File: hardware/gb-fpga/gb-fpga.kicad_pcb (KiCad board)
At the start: 4 copper layers, 80.1 x 78.6 mm, 20 parts, among them J1 USB_C_Receptacle_USB2.0, J2 Cartridge-32pin, U1 xc7s25ftgb196, U2 MX25R3235FZBxx1, U3 FT2232HQ

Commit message: Add USB connections
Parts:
- added R10: 10k, Resistor_SMD:R_0603_1608Metric, F.Cu at (11.0, -48.4)
- added R11: 10k, Resistor_SMD:R_0603_1608Metric, F.Cu at (11.0, -45.9)
- added R12: 10k, Resistor_SMD:R_0603_1608Metric, F.Cu at (15.0, -48.4)
- added R13: 10k, Resistor_SMD:R_0603_1608Metric, F.Cu at (11.0, -43.3)
- added R14: 12k, Resistor_SMD:R_0603_1608Metric, F.Cu at (15.0, -45.9)
- added R15: 1k, Resistor_SMD:R_0603_1608Metric, F.Cu at (19.0, -48.4)
- added R16: 4.7k, Resistor_SMD:R_0603_1608Metric, F.Cu at (15.0, -43.3)
- added R17: 4.7k, Resistor_SMD:R_0603_1608Metric, F.Cu at (19.0, -45.9)
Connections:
- J1 pad A1: Net-(J1-PadA1) -> GND
- J1 pad A12: Net-(J1-PadA1) -> GND
- J1 pad B1: Net-(J1-PadA1) -> GND
- J1 pad B12: Net-(J1-PadA1) -> GND
- J1 pad B6: Net-(J1-PadB6) -> Net-(J1-PadA6)
- J1 pad B7: Net-(J1-PadB7) -> Net-(J1-PadA7)
- J1 pad S1: Net-(J1-PadS1) -> GND
- U1 pad A12: (no net) -> Net-(U1-PadA12)
- U1 pad A13: (no net) -> Net-(U1-PadA13)
- U1 pad A2: (no net) -> Net-(U1-PadA2)
- U1 pad A3: (no net) -> Net-(U1-PadA3)
- U1 pad A4: (no net) -> Net-(U1-PadA4)
- U1 pad A5: (no net) -> Net-(U1-PadA5)
- U1 pad A7: Net-(U1-PadA7) -> TCK
- U1 pad B1: (no net) -> Net-(U1-PadB1)
- U1 pad B13: (no net) -> Net-(U1-PadB13)
- U1 pad B14: (no net) -> Net-(U1-PadB14)
- U1 pad B2: (no net) -> Net-(U1-PadB2)
- U1 pad B3: (no net) -> Net-(U1-PadB3)
- U1 pad B5: (no net) -> Net-(U1-PadB5)
- U1 pad B6: (no net) -> Net-(U1-PadB6)
- U1 pad C1: (no net) -> Net-(U1-PadC1)
- U1 pad C12: (no net) -> Net-(U1-PadC12)
- U1 pad C14: (no net) -> Net-(U1-PadC14)
- U1 pad C3: (no net) -> Net-(U1-PadC3)
- U1 pad C4: (no net) -> Net-(U1-PadC4)
- U1 pad C5: (no net) -> Net-(U1-PadC5)
- U1 pad D1: (no net) -> Net-(U1-PadD1)
- U1 pad D12: (no net) -> Net-(U1-PadD12)
- U1 pad D13: (no net) -> Net-(U1-PadD13)
- U1 pad D14: (no net) -> Net-(U1-PadD14)
- U1 pad D2: (no net) -> Net-(U1-PadD2)
- U1 pad D3: (no net) -> Net-(U1-PadD3)
- U1 pad D4: (no net) -> Net-(U1-PadD4)
- U1 pad E11: (no net) -> Net-(U1-PadE11)
- U1 pad E12: (no net) -> Net-(U1-PadE12)
- U1 pad E13: (no net) -> Net-(U1-PadE13)
- U1 pad E2: (no net) -> Net-(U1-PadE2)
- U1 pad E4: (no net) -> Net-(U1-PadE4)
- U1 pad F1: (no net) -> RX
- U1 pad F11: (no net) -> Net-(U1-PadF11)
- U1 pad F12: (no net) -> Net-(U1-PadF12)
- U1 pad F13: (no net) -> Net-(U1-PadF13)
- U1 pad F14: (no net) -> Net-(U1-PadF14)
- U1 pad F2: (no net) -> Net-(U1-PadF2)
- U1 pad F3: (no net) -> Net-(U1-PadF3)
- U1 pad F4: (no net) -> Net-(U1-PadF4)
- U1 pad G1: (no net) -> TX
- U1 pad G11: (no net) -> Net-(U1-PadG11)
- U1 pad G14: (no net) -> Net-(U1-PadG14)
- U1 pad G4: (no net) -> Net-(U1-PadG4)
- U1 pad H1: (no net) -> Net-(U1-PadH1)
- U1 pad H11: (no net) -> Net-(U1-PadH11)
- U1 pad H12: (no net) -> Net-(U1-PadH12)
- U1 pad H13: (no net) -> Net-(U1-PadH13)
- U1 pad H14: (no net) -> Net-(U1-PadH14)
- U1 pad H2: (no net) -> Net-(U1-PadH2)
- U1 pad H3: (no net) -> Net-(U1-PadH3)
- U1 pad H4: (no net) -> Net-(U1-PadH4)
- U1 pad J1: (no net) -> Net-(U1-PadJ1)
- U1 pad J11: (no net) -> Net-(U1-PadJ11)
- U1 pad J12: (no net) -> Net-(U1-PadJ12)
- U1 pad J13: (no net) -> Net-(U1-PadJ13)
- U1 pad J14: (no net) -> Net-(U1-PadJ14)
- U1 pad J2: (no net) -> Net-(U1-PadJ2)
- U1 pad J3: (no net) -> Net-(U1-PadJ3)
- U1 pad J4: (no net) -> Net-(U1-PadJ4)
- U1 pad K11: (no net) -> Net-(U1-PadK11)
- U1 pad K12: (no net) -> Net-(U1-PadK12)
- U1 pad K3: (no net) -> Net-(U1-PadK3)
- U1 pad K4: (no net) -> Net-(U1-PadK4)
- U1 pad L1: (no net) -> Net-(U1-PadL1)
- U1 pad L12: (no net) -> Net-(U1-PadL12)
- U1 pad L13: (no net) -> Net-(U1-PadL13)
- U1 pad L14: (no net) -> Net-(U1-PadL14)
- U1 pad L2: (no net) -> Net-(U1-PadL2)
- U1 pad L3: (no net) -> Net-(U1-PadL3)
- U1 pad L5: (no net) -> Net-(U1-PadL5)
- U1 pad M1: (no net) -> Net-(U1-PadM1)
- U1 pad M10: (no net) -> Net-(U1-PadM10)
- U1 pad M11: (no net) -> Net-(U1-PadM11)
- U1 pad M12: (no net) -> Net-(U1-PadM12)
- U1 pad M13: (no net) -> Net-(U1-PadM13)
- U1 pad M14: (no net) -> Net-(U1-PadM14)
- U1 pad M2: (no net) -> Net-(U1-PadM2)
- U1 pad M3: (no net) -> Net-(U1-PadM3)
- U1 pad M4: (no net) -> Net-(U1-PadM4)
- U1 pad M5: (no net) -> Net-(U1-PadM5)
- U1 pad M6: Net-(U1-PadM6) -> TMS
- U1 pad N1: (no net) -> Net-(U1-PadN1)
- U1 pad N10: (no net) -> Net-(U1-PadN10)
- U1 pad N11: (no net) -> Net-(U1-PadN11)
- U1 pad N14: (no net) -> Net-(U1-PadN14)
- U1 pad N4: (no net) -> Net-(U1-PadN4)
- U1 pad P10: (no net) -> Net-(U1-PadP10)
- U1 pad P11: (no net) -> Net-(U1-PadP11)
- U1 pad P12: (no net) -> Net-(U1-PadP12)
- U1 pad P13: (no net) -> Net-(U1-PadP13)
- U1 pad P2: (no net) -> Net-(U1-PadP2)
- U1 pad P3: (no net) -> Net-(U1-PadP3)
- U1 pad P4: (no net) -> Net-(U1-PadP4)
- U1 pad P5: (no net) -> Net-(U1-PadP5)
- U1 pad P6: Net-(U1-PadP6) -> TDO
- U1 pad P7: Net-(U1-PadP7) -> TDI
- U3 pad 10: Net-(U3-Pad10) -> GND
- U3 pad 13: Net-(U3-Pad13) -> GND
- U3 pad 16: Net-(U3-Pad16) -> TCK
- U3 pad 17: Net-(U3-Pad17) -> TDI
- U3 pad 18: Net-(U3-Pad18) -> TDO
- U3 pad 19: Net-(U3-Pad19) -> TMS
- U3 pad 38: Net-(U3-Pad38) -> TX
- U3 pad 39: Net-(U3-Pad39) -> RX
- U3 pad 7: Net-(U3-Pad7) -> Net-(J1-PadA7)
- U3 pad 8: Net-(U3-Pad8) -> Net-(J1-PadA6)

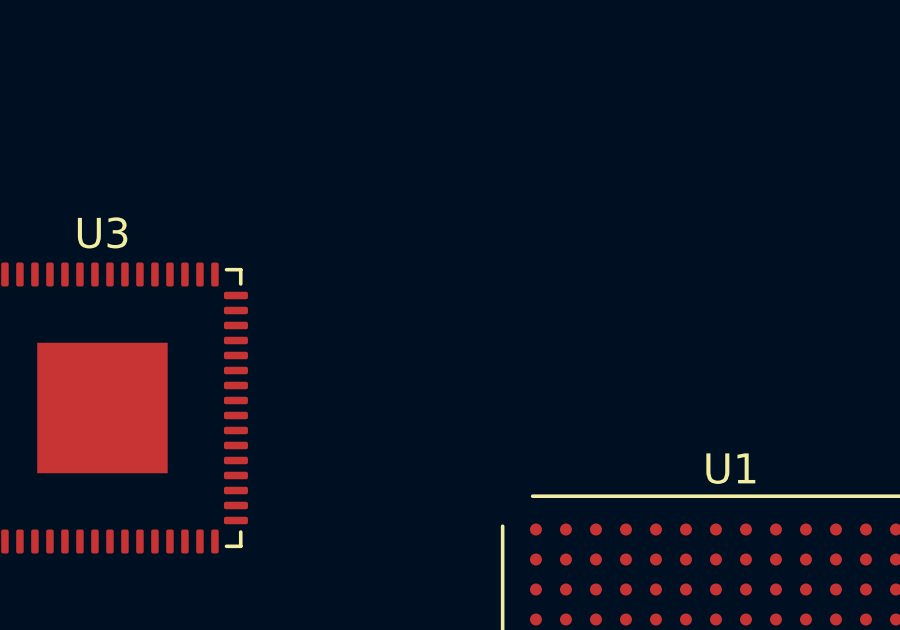
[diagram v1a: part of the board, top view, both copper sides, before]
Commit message: Add oscillator
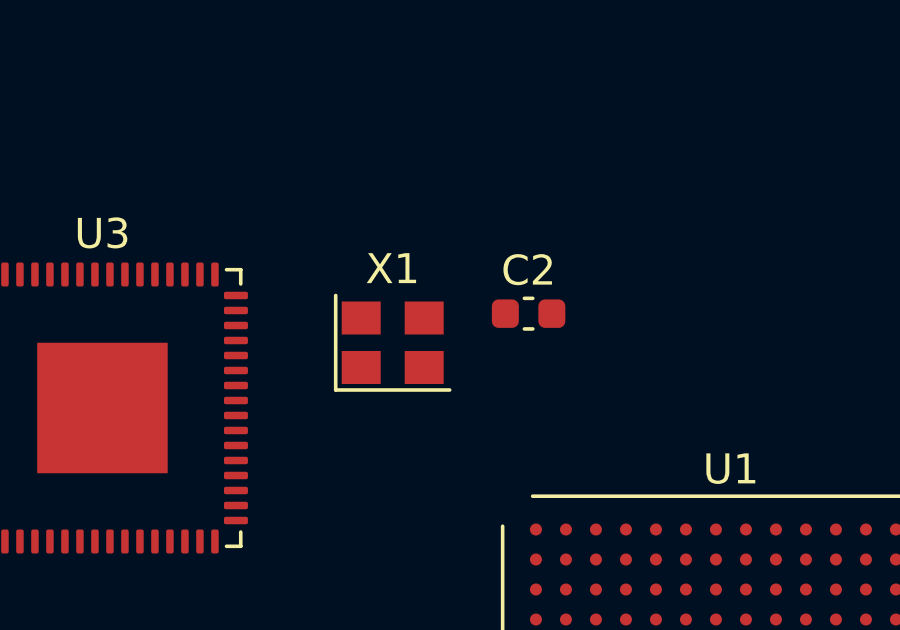
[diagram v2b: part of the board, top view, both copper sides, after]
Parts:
- added C2: 10nF, Capacitor_SMD:C_0603_1608Metric, F.Cu at (33.1, -61.1)
- added X1: SG-8002JA, Oscillator:Oscillator_SMD_Abracon_ASE-4Pin_3.2x2.5mm, F.Cu at (28.6, -60.1)
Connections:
- U1 pad H3: Net-(U1-PadH3) -> 12MHZ
- U3 pad 2: Net-(U3-Pad2) -> 12MHZ

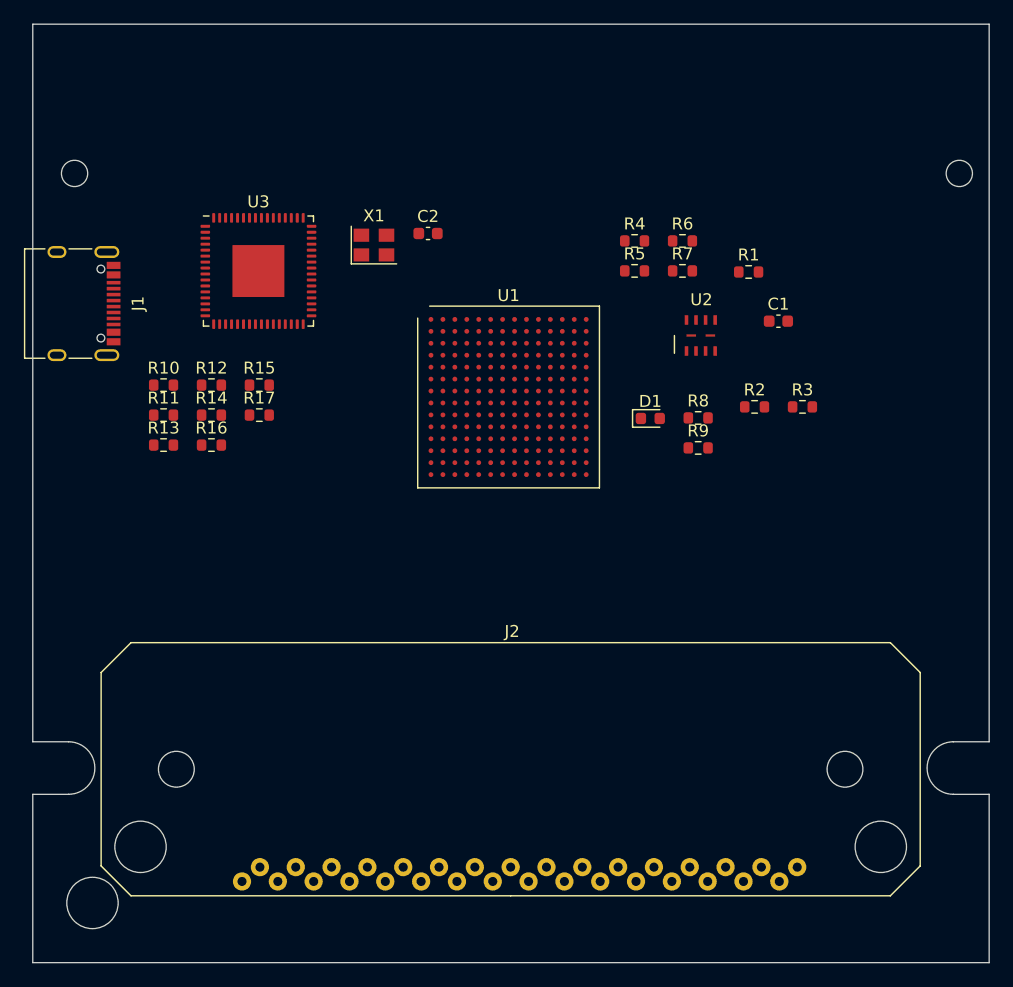
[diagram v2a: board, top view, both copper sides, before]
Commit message: Add LTC3555
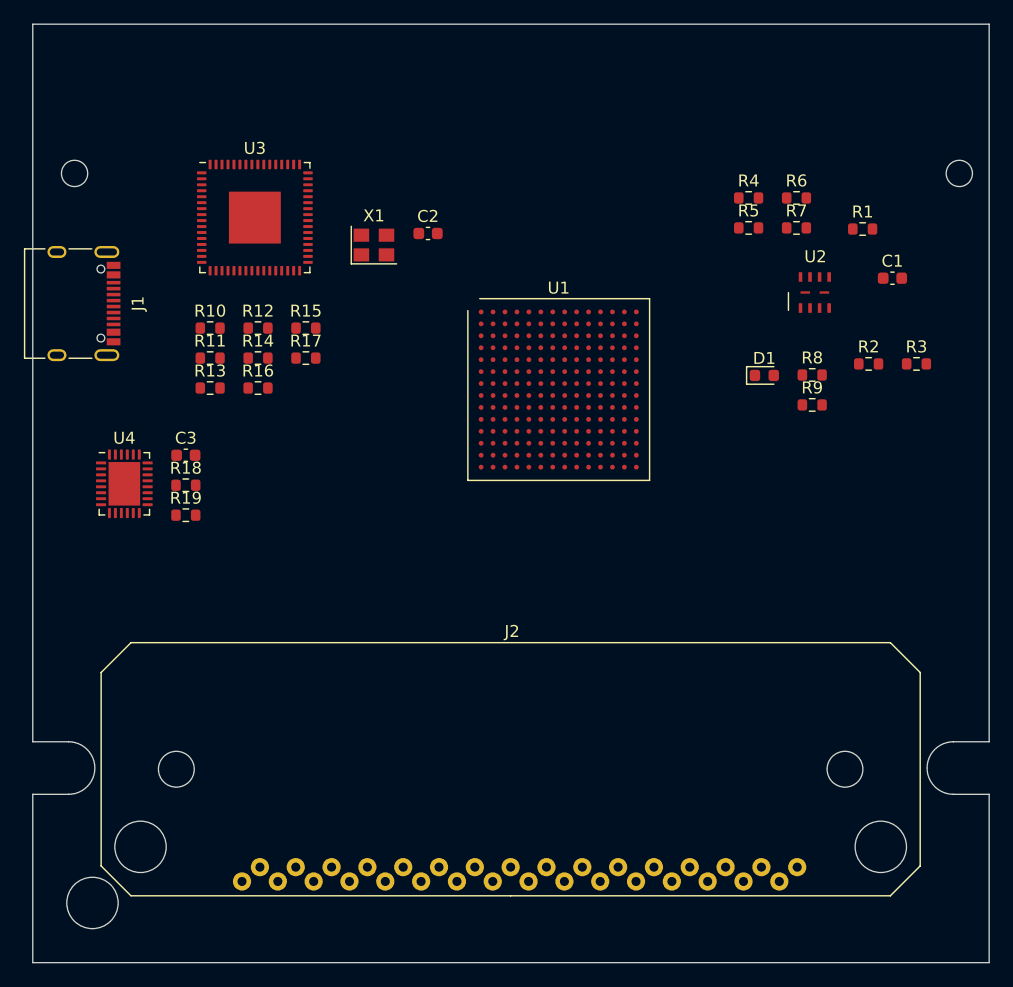
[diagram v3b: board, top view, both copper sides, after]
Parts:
- added C3: 470nF, Capacitor_SMD:C_0603_1608Metric, F.Cu at (12.8, -42.5)
- added R18: 3k, Resistor_SMD:R_0603_1608Metric, F.Cu at (12.8, -40.0)
- added R19: 2k, Resistor_SMD:R_0603_1608Metric, F.Cu at (12.8, -37.5)
- added U4: LTC3555, Package_DFN_QFN:QFN-28-1EP_4x5mm_P0.5mm_EP2.65x3.65mm, F.Cu at (7.67, -40.1)
- moved R4 10.2 mm to (60.0, -64.0)
- moved R5 10.2 mm to (60.0, -61.5)
- moved R6 10.2 mm to (64.0, -64.0)
- moved R7 10.2 mm to (64.0, -61.5)
- moved C1 10.2 mm to (72.0, -57.3)
- moved D1 10.2 mm to (61.3, -49.2)
- moved R3 10.2 mm to (74.0, -50.1)
- moved R8 10.2 mm to (65.3, -49.2)
- moved R9 10.2 mm to (65.3, -46.7)
- moved U2 10.2 mm to (65.5, -56.1)
- moved R1 10.2 mm to (69.5, -61.4)
- moved R2 10.2 mm to (70.0, -50.1)
- moved R13 6.17 mm to (14.9, -48.1)
- moved R16 6.17 mm to (18.9, -48.1)
- moved R15 6.17 mm to (22.9, -53.1)
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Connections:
- net Net-(J1-PadA4) renamed USB_5V
- net Net-(J2-Pad1) renamed +5V
- net Net-(J2-Pad10) renamed GB_A4
- net Net-(J2-Pad11) renamed GB_A5
- net Net-(J2-Pad12) renamed GB_A6
- net Net-(J2-Pad13) renamed GB_A7
- net Net-(J2-Pad14) renamed GB_A8
- net Net-(J2-Pad15) renamed GB_A9
- net Net-(J2-Pad16) renamed GB_A10
- net Net-(J2-Pad17) renamed GB_A11
- net Net-(J2-Pad18) renamed GB_A12
- net Net-(J2-Pad19) renamed GB_A13
- net Net-(J2-Pad20) renamed GB_A14
- net Net-(J2-Pad21) renamed GB_CS
- net Net-(J2-Pad22) renamed GB_D0
- net Net-(J2-Pad23) renamed GB_D1
- net Net-(J2-Pad24) renamed GB_D2
- net Net-(J2-Pad25) renamed GB_D3
- net Net-(J2-Pad26) renamed GB_D4
- net Net-(J2-Pad27) renamed GB_D5
- net Net-(J2-Pad28) renamed GB_D6
- net Net-(J2-Pad29) renamed GB_D7
- net Net-(J2-Pad3) renamed GB_RST
- net Net-(J2-Pad30) renamed GB_RD
- net Net-(J2-Pad4) renamed GB_WR
- net Net-(J2-Pad6) renamed GB_A0
- net Net-(J2-Pad7) renamed GB_A1
- net Net-(J2-Pad8) renamed GB_A2
- net Net-(J2-Pad9) renamed GB_A3

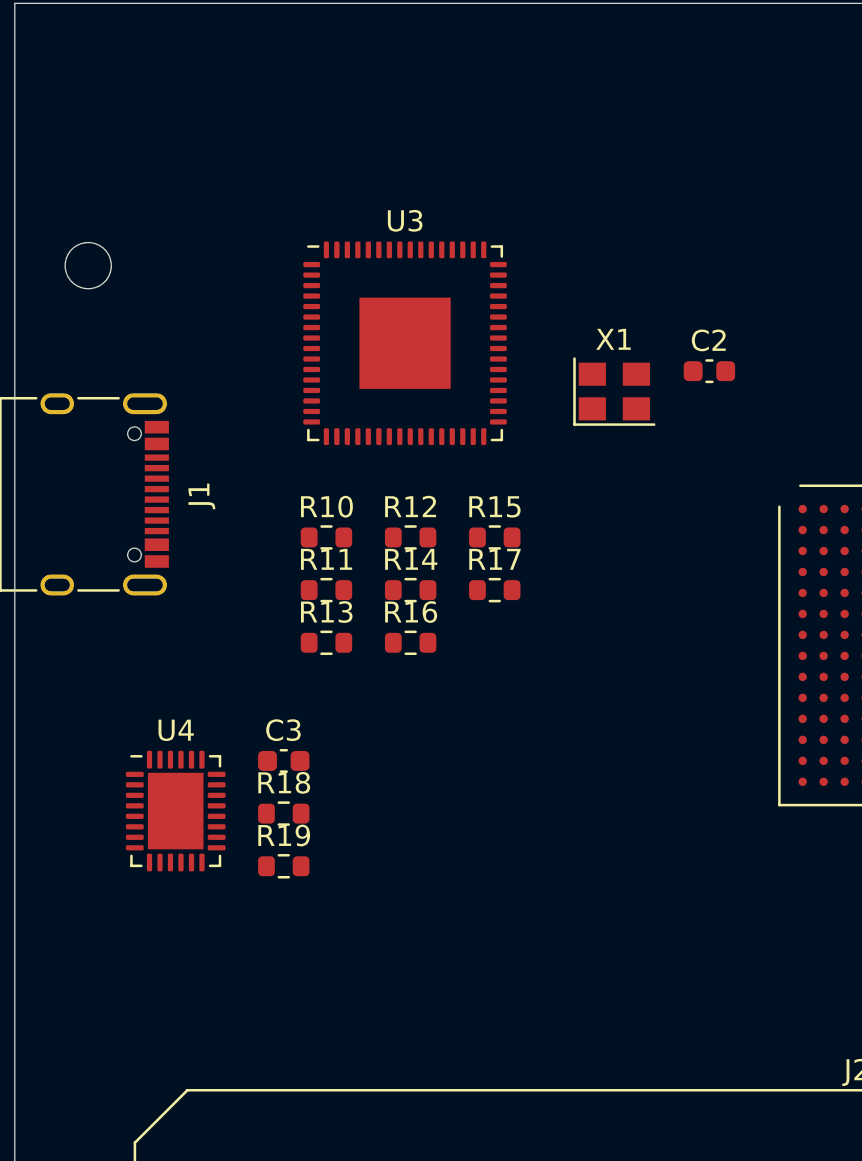
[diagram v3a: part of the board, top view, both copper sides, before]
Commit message: Add step-down conversion
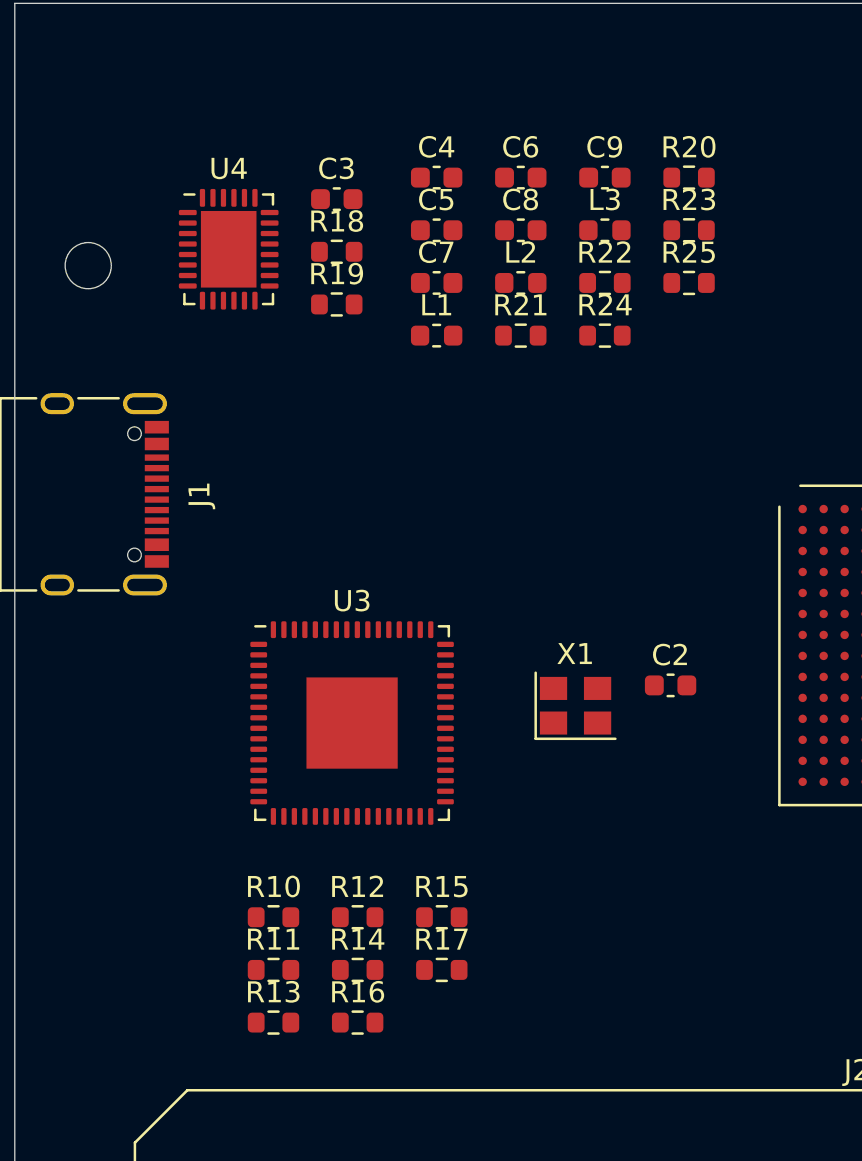
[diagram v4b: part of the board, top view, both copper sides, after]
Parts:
- added C4: 20pF, Capacitor_SMD:C_0603_1608Metric, F.Cu at (20.1, -70.3)
- added C5: 22µF, Capacitor_SMD:C_0603_1608Metric, F.Cu at (20.1, -67.8)
- added C6: 20pF, Capacitor_SMD:C_0603_1608Metric, F.Cu at (24.1, -70.3)
- added C7: 10µF, Capacitor_SMD:C_0603_1608Metric, F.Cu at (20.1, -65.3)
- added C8: 20pF, Capacitor_SMD:C_0603_1608Metric, F.Cu at (24.1, -67.8)
- added C9: 10µF, Capacitor_SMD:C_0603_1608Metric, F.Cu at (28.1, -70.3)
- added L1: 1.5µH, Inductor_SMD:L_0603_1608Metric, F.Cu at (20.1, -62.8)
- added L2: 3.3µH, Inductor_SMD:L_0603_1608Metric, F.Cu at (24.1, -65.3)
- added L3: 2.2µH, Inductor_SMD:L_0603_1608Metric, F.Cu at (28.1, -67.8)
- added R20: 30k, Resistor_SMD:R_0603_1608Metric, F.Cu at (32.1, -70.3)
- added R21: 120k, Resistor_SMD:R_0603_1608Metric, F.Cu at (24.1, -62.8)
- added R22: 150k, Resistor_SMD:R_0603_1608Metric, F.Cu at (28.1, -65.3)
- added R23: 120k, Resistor_SMD:R_0603_1608Metric, F.Cu at (32.1, -67.8)
- added R24: 180k, Resistor_SMD:R_0603_1608Metric, F.Cu at (28.1, -62.8)
- added R25: 57.6k, Resistor_SMD:R_0603_1608Metric, F.Cu at (32.1, -65.3)
- moved R19 26.9 mm to (15.3, -64.2)
- moved C3 26.9 mm to (15.3, -69.3)
- moved U4 26.9 mm to (10.2, -66.9)
- moved R18 26.9 mm to (15.3, -66.8)
- moved R10 18.3 mm to (12.3, -35.0)
- moved R11 18.3 mm to (12.3, -32.5)
- moved R12 18.3 mm to (16.3, -35.0)
- moved R13 18.3 mm to (12.3, -30.0)
- moved R14 18.3 mm to (16.3, -32.5)
- moved R15 18.3 mm to (20.4, -35.0)
- moved R16 18.3 mm to (16.3, -30.0)
- moved R17 18.3 mm to (20.4, -32.5)
- moved U3 18.3 mm to (16.1, -44.3)
- moved C2 15.1 mm to (31.3, -46.1)
- moved X1 15.1 mm to (26.7, -45.1)

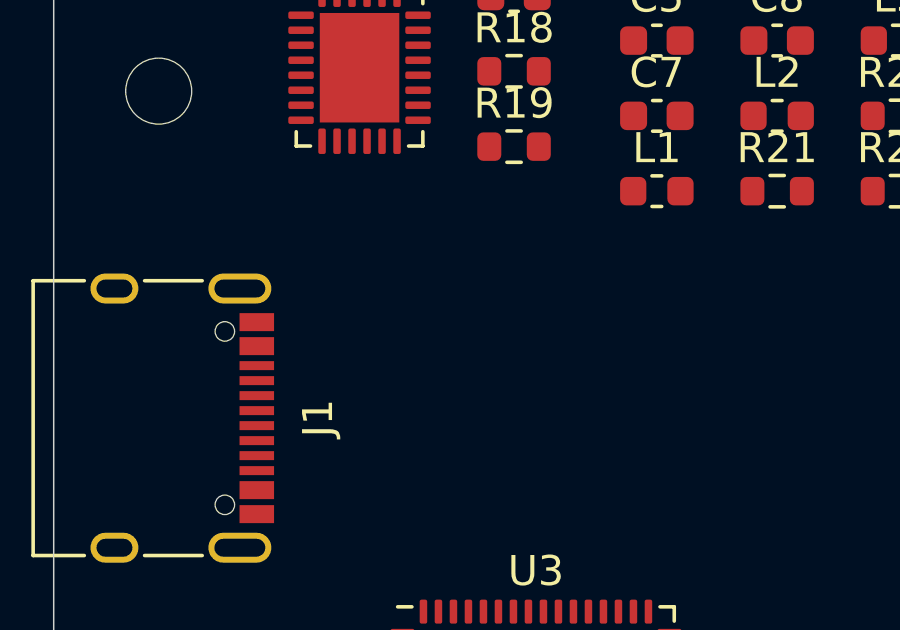
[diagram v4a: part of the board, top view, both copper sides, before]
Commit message: Add reverse polarity protection to usb
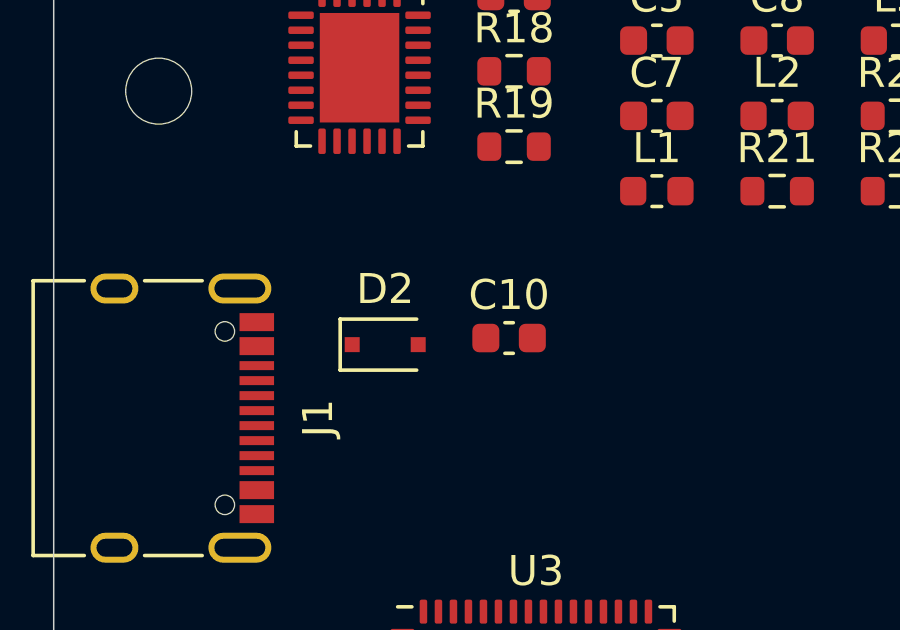
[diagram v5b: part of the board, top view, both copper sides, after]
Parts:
- added C10: 100nF, Capacitor_SMD:C_0603_1608Metric, F.Cu at (15.2, -57.9)
- added D2: PMEG2020EJ, Diode_SMD:D_SOD-323F, F.Cu at (11.1, -57.6)
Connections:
- J1 pad A4: USB_5V -> Net-(C10-Pad1)
- J1 pad A9: USB_5V -> Net-(C10-Pad1)
- J1 pad B4: USB_5V -> Net-(C10-Pad1)
- J1 pad B9: USB_5V -> Net-(C10-Pad1)
